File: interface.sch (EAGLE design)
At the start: 17 parts, among them U1 ATMEGA328P_PDIP

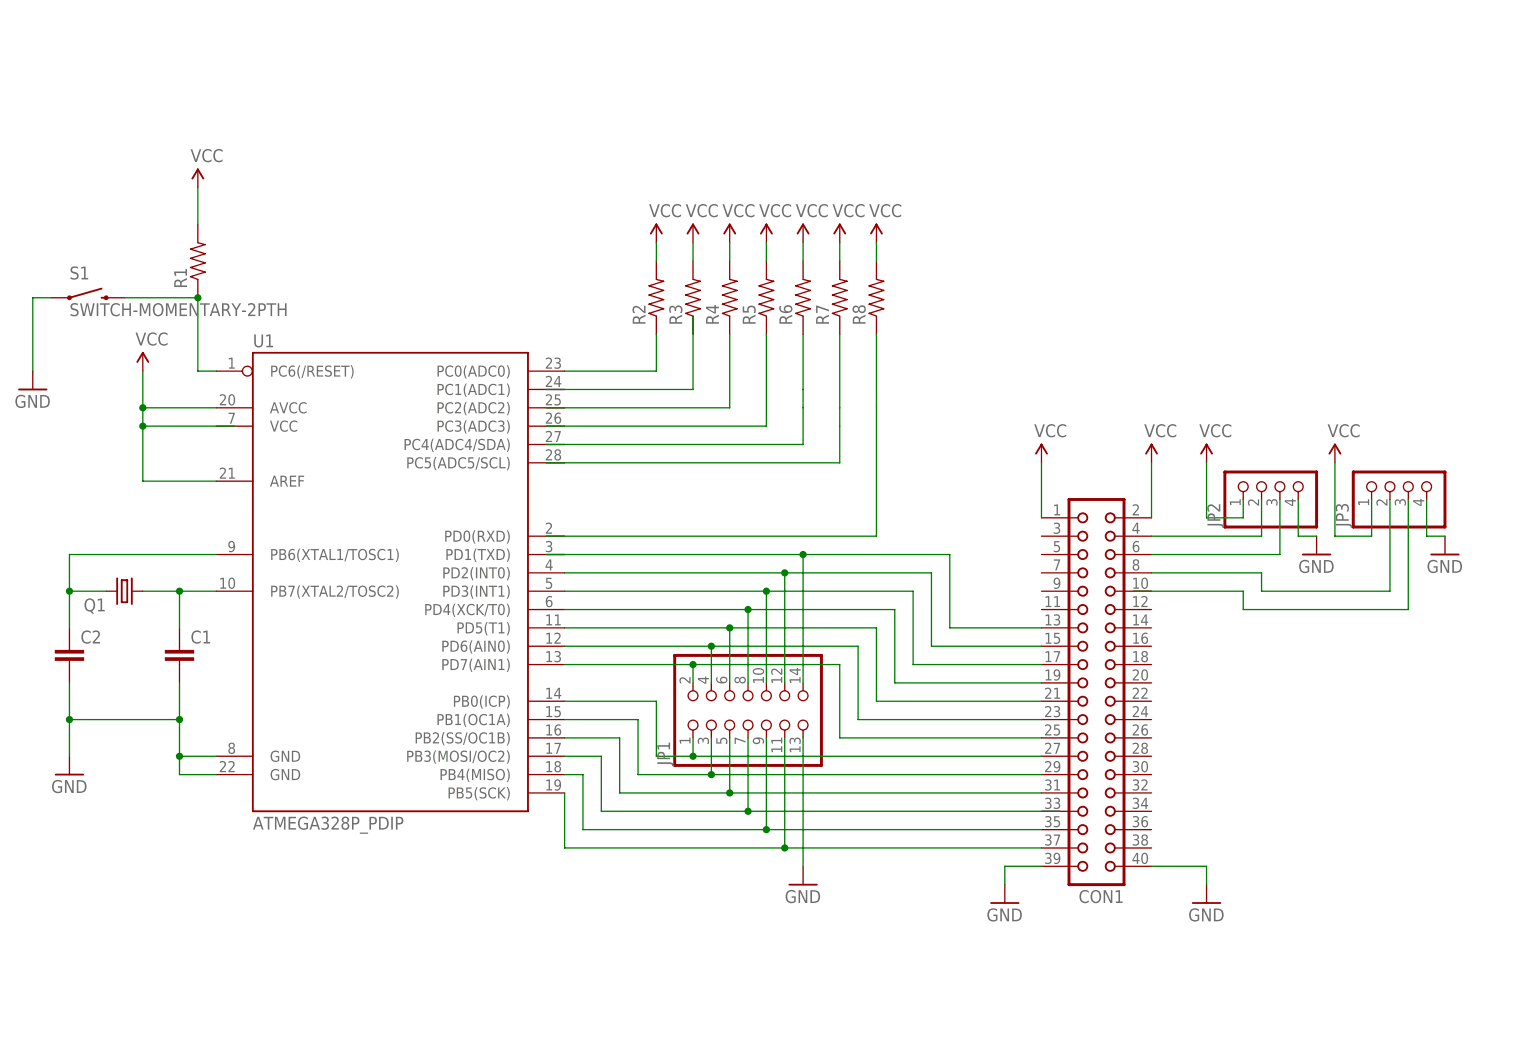
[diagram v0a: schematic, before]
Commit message: Rough draft on schematic complete. Checklist of areas to check created
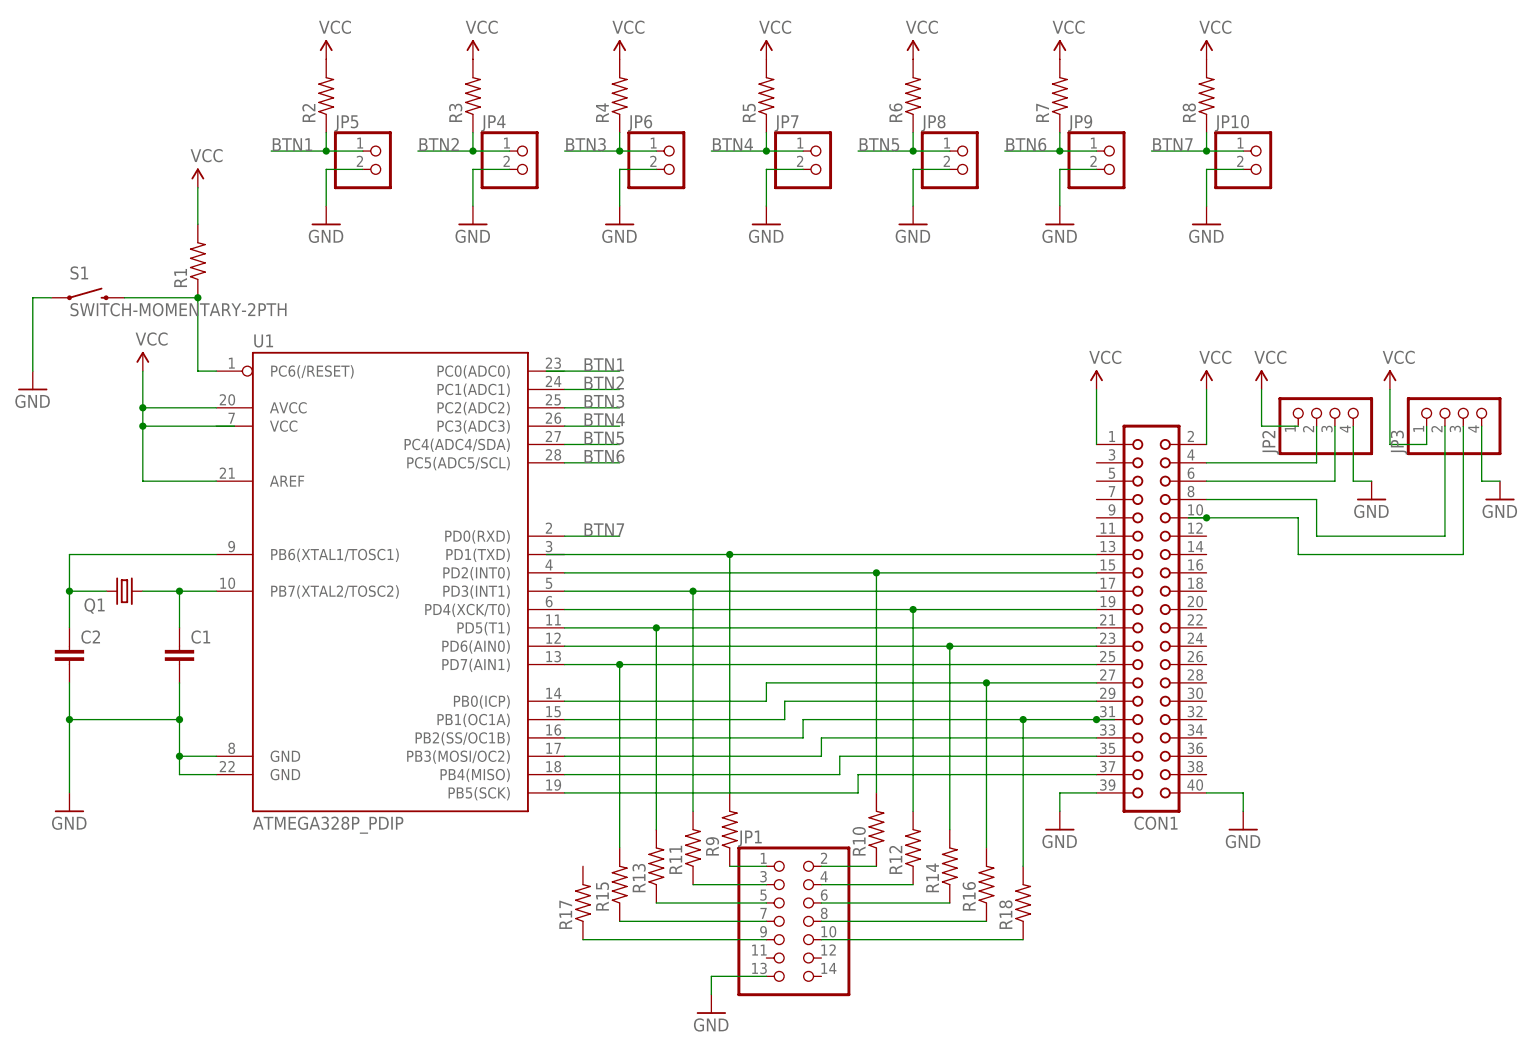
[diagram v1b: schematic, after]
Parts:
- added JP10, JP4, JP5, JP6, JP7, JP8, JP9: (no value), pinhead:PINHD-1X2
- added R10, R11, R12, R13, R14, R15, R16, R17, R18, R9: (no value), SparkFun-Passives:RESISTORPTH-1/4W
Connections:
- new net BTN1: JP5.1, R2.1
- new net BTN2: JP4.1, R3.1, U1.PC1(ADC1)
- new net BTN3: JP6.1, R4.1, U1.PC2(ADC2)
- new net BTN4: JP7.1, R5.1, U1.PC3(ADC3)
- new net BTN5: JP8.1, R6.1, U1.PC4(ADC4/SDA)
- new net BTN6: JP9.1, R7.1, U1.PC5(ADC5/SCL)
- new net BTN7: JP10.1, R8.1, U1.PD0(RXD)
- new net N$24: JP1.4, R12.1
- new net N$28: JP1.8, R16.1
- new net N$29: JP1.9, R17.1
- new net N$30: JP1.10, R18.1
- net GND: now also JP10.2, JP4.2, JP5.2, JP6.2, JP7.2, JP8.2, JP9.2
- net N$10: now also R15.2; no longer JP1.2
- net N$11: now also R14.2; no longer JP1.4
- net N$12: now also R13.2; no longer JP1.6
- net N$13: now also CON1.19, R12.2; no longer JP1.8
- net N$14: now also R11.2; no longer JP1.10
- net N$15: now also CON1.15, R10.2; no longer JP1.12
- net N$16: now also R9.2; no longer JP1.14
- net N$18: now also CON1.10
- net N$21: now also JP1.1, R9.1; no longer R2.1, U1.PC0(ADC0)
- net N$22: now also JP1.2, R10.1; no longer R6.1
- net N$23: now also JP1.3, R11.1; no longer R4.1
- net N$25: now also JP1.5, R13.1; no longer R5.1
- net N$26: now also JP1.6, R14.1; no longer R7.1
- net N$27: now also JP1.7, R15.1; no longer R8.1
- net N$4: now also R16.2; no longer JP1.1
- net N$5: no longer JP1.3
- net N$6: now also CON1.31, R18.2; no longer JP1.5
- net N$7: now also CON1.33; no longer JP1.7
- net N$8: now also CON1.35; no longer JP1.9
- net N$9: no longer JP1.11
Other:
- moved on the sheet: CON1, JP1, JP2, JP3, R2, R3, R4, R5, R6, R7, R8

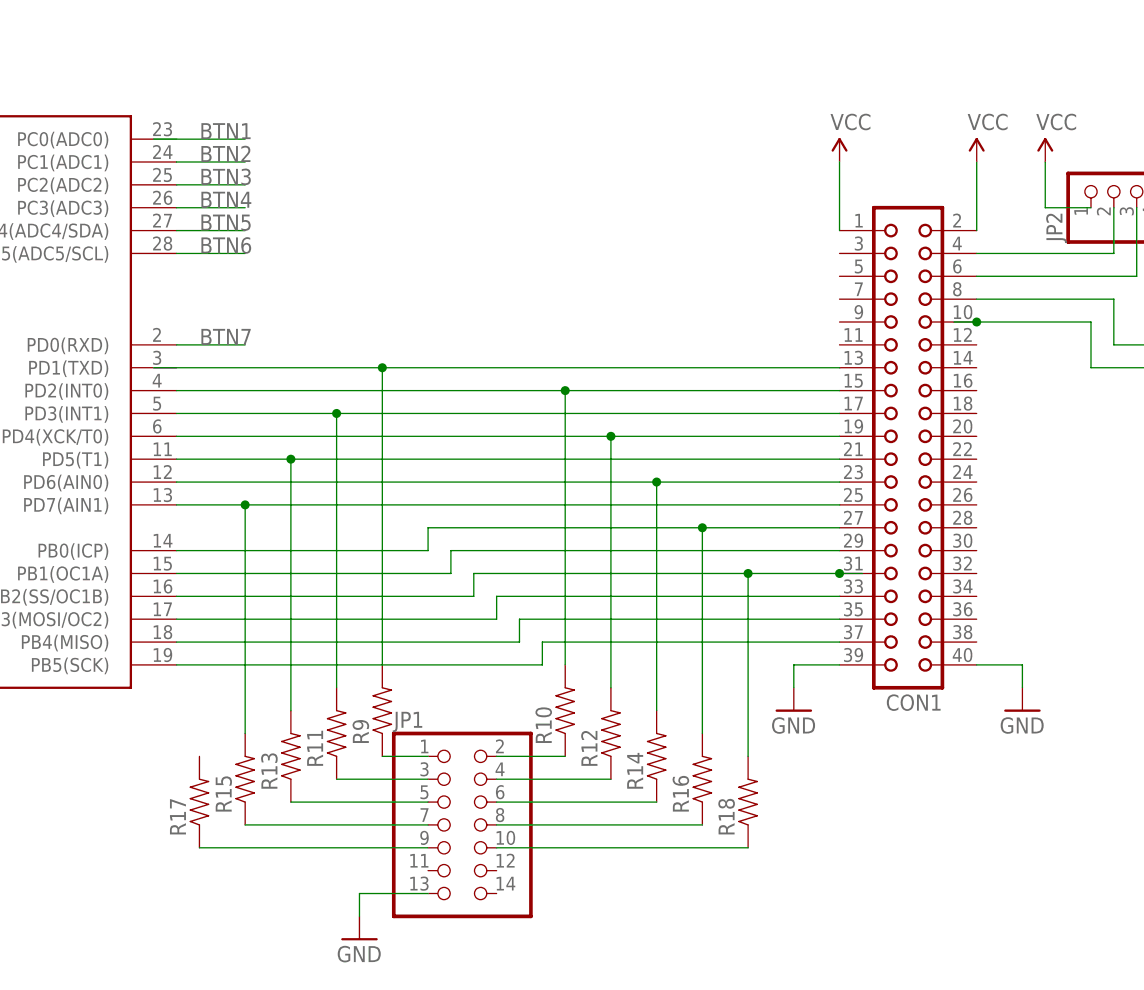
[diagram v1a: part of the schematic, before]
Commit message: Started layout
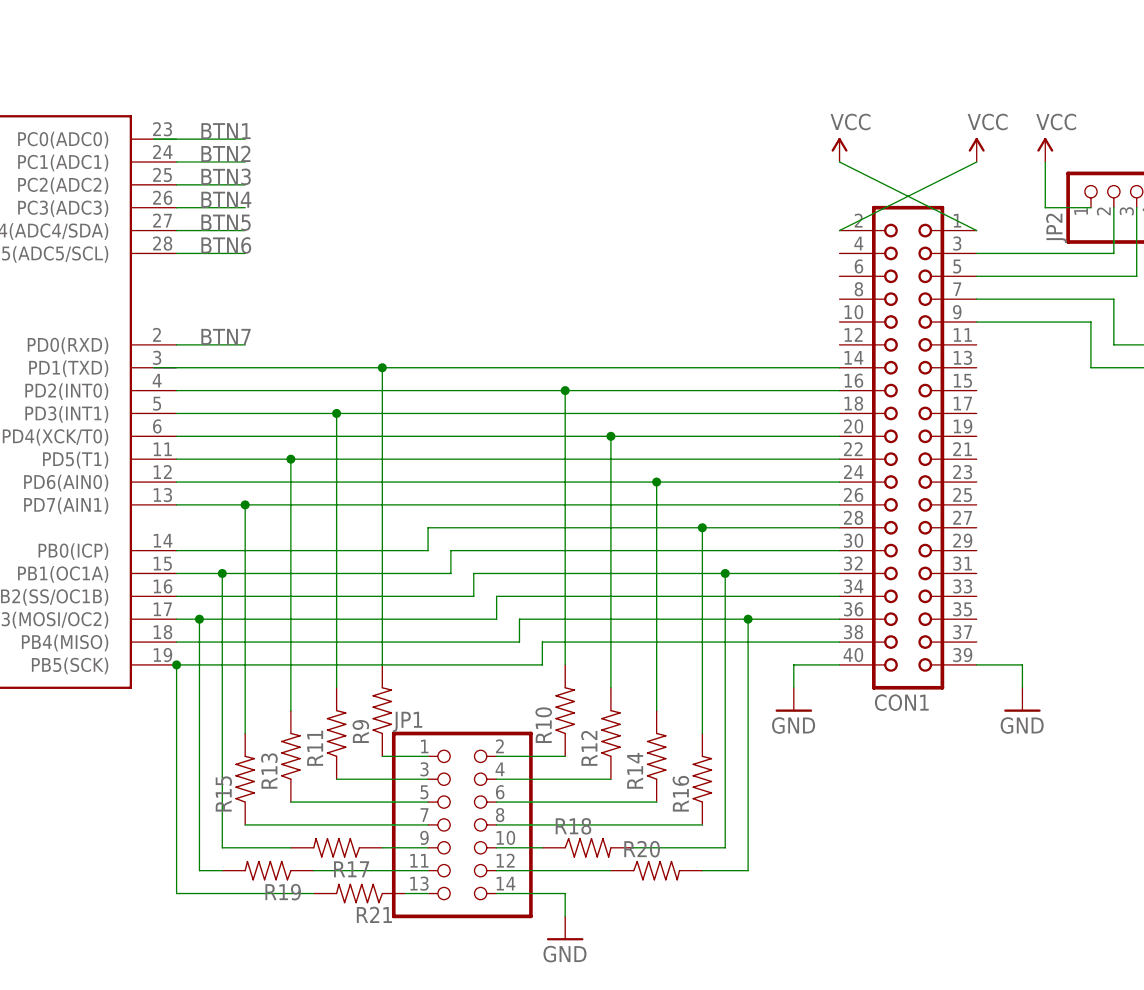
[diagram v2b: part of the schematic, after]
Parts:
- added R19, R20, R21: (no value), SparkFun-Passives:RESISTORPTH-1/4W
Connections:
- new net N$31: JP1.11, R19.1
- new net N$32: JP1.12, R20.1
- new net N$33: JP1.13, R21.1
- net GND: now also JP1.14; no longer JP1.13
- net N$10: now also CON1.26; no longer CON1.25
- net N$11: now also CON1.24; no longer CON1.23
- net N$12: now also CON1.22; no longer CON1.21
- net N$13: now also CON1.20; no longer CON1.19
- net N$14: now also CON1.18; no longer CON1.17
- net N$15: now also CON1.16; no longer CON1.15
- net N$16: now also CON1.14; no longer CON1.13
- net N$17: now also CON1.7; no longer CON1.8
- net N$18: now also CON1.9; no longer CON1.10
- net N$19: now also CON1.5; no longer CON1.6
- net N$20: now also CON1.3; no longer CON1.4
- net N$4: now also CON1.28; no longer CON1.27
- net N$5: now also CON1.30, R17.2; no longer CON1.29
- net N$6: now also CON1.32; no longer CON1.31
- net N$7: now also CON1.34, R19.2; no longer CON1.33
- net N$8: now also CON1.36, R20.2; no longer CON1.35
- net N$9: now also CON1.38, R21.2; no longer CON1.37
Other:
- moved on the sheet: R17, R18
